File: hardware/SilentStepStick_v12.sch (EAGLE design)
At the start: 30 parts, among them IC1 TMC2100_QFN36, X1 PASSER-07, X2 PASSER-07

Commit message: updated layout and schematics
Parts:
- C8: value C0603/1uF/50V -> 1u/50V
- IC1: value TMC2100_QFN36 -> TMC2100-LA; device TMC2100_QFN:TMC2100_QFN36 -> we-chip:TMC2100-LA
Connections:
- net N$7 renamed BRA
- net N$9 renamed BRB
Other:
- moved on the sheet: C1, C2, C3, C4, C5, C6, C7, C8, JP1, JP2, JP3, JP4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

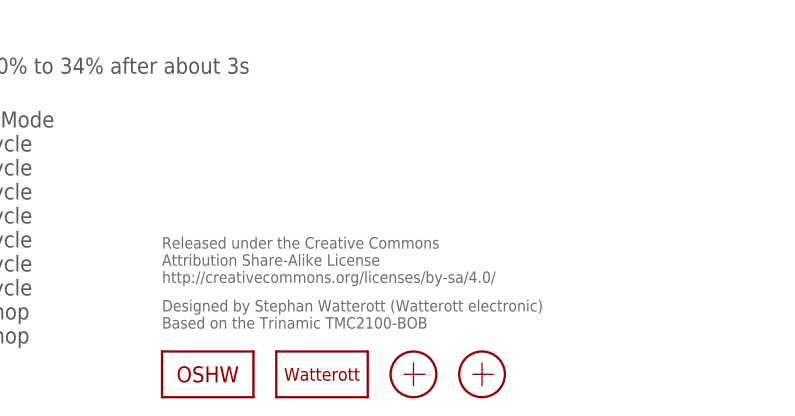
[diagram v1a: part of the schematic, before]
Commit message: updated schematics
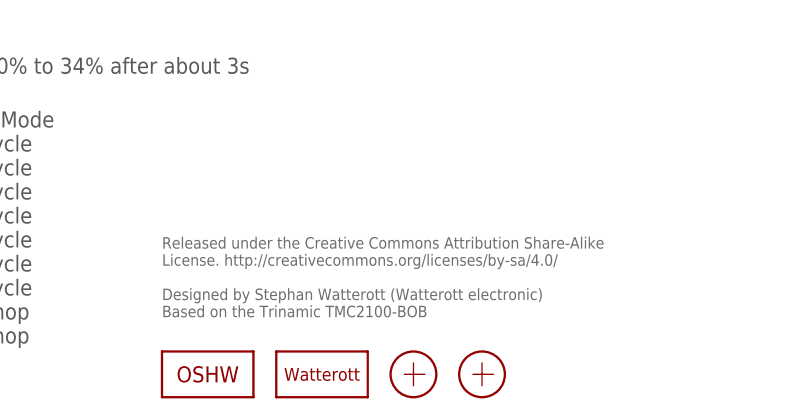
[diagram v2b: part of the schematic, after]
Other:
- note added: "Released under the Creative Commons Attribution Share-Alike License. http://creativecommons.org/licenses/by-sa/4.0/ Designed by Stephan Watterott (Watterott electronic) Based on the Trinamic TMC2100-BOB"
- note removed: "Designed by Stephan Watterott (Watterott electronic) Based on the Trinamic TMC2100-BOB"
- note removed: "Released under the Creative Commons Attribution Share-Alike License http://creativecommons.org/licenses/by-sa/4.0/"
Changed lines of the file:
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@@
 <setting verticaltext="up"/>
 </settings>
-<grid distance="0.1" unitdist="inch" unit="inch" style="lines" multiple="1" display="no" altdistance="0.01" altunitdist="inch" altunit="inch"/>
+<grid distance="0.05" unitdist="inch" unit="inch" style="lines" multiple="1" display="yes" altdistance="0.025" altunitdist="inch" altunit="inch"/>
 <layers>
 <layer number="1" name="Top" color="4" fill="1" visible="no" active="no"/>
@@
 <wire x1="16.51" y1="33.02" x2="16.51" y2="35.56" width="1.016" layer="94"/>
 <wire x1="16.51" y1="17.78" x2="16.51" y2="20.32" width="1.016" layer="94"/>
-<text x="162.56" y="17.78" size="1.27" layer="95">Released under the Creative Commons
-Attribution Share-Alike License
-http://creativecommons.org/licenses/by-sa/4.0/</text>
-<text x="162.56" y="12.7" size="1.27" layer="95">Designed by Stephan Watterott (Watterott electronic)
+<text x="162.56" y="22.86" size="1.27" layer="95" align="top-left">Released under the Creative Commons Attribution Share-Alike
+License. http://creativecommons.org/licenses/by-sa/4.0/
+Designed by Stephan Watterott (Watterott electronic)
 Based on the Trinamic TMC2100-BOB</text>
 <text x="90.17" y="50.8" size="1.778" layer="97" font="vector" ratio="10" align="top-left">CFG6/En
